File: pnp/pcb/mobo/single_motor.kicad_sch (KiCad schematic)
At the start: 9 parts, among them J26 TMC_PIN_HEADER, M2 Stepper_Motor

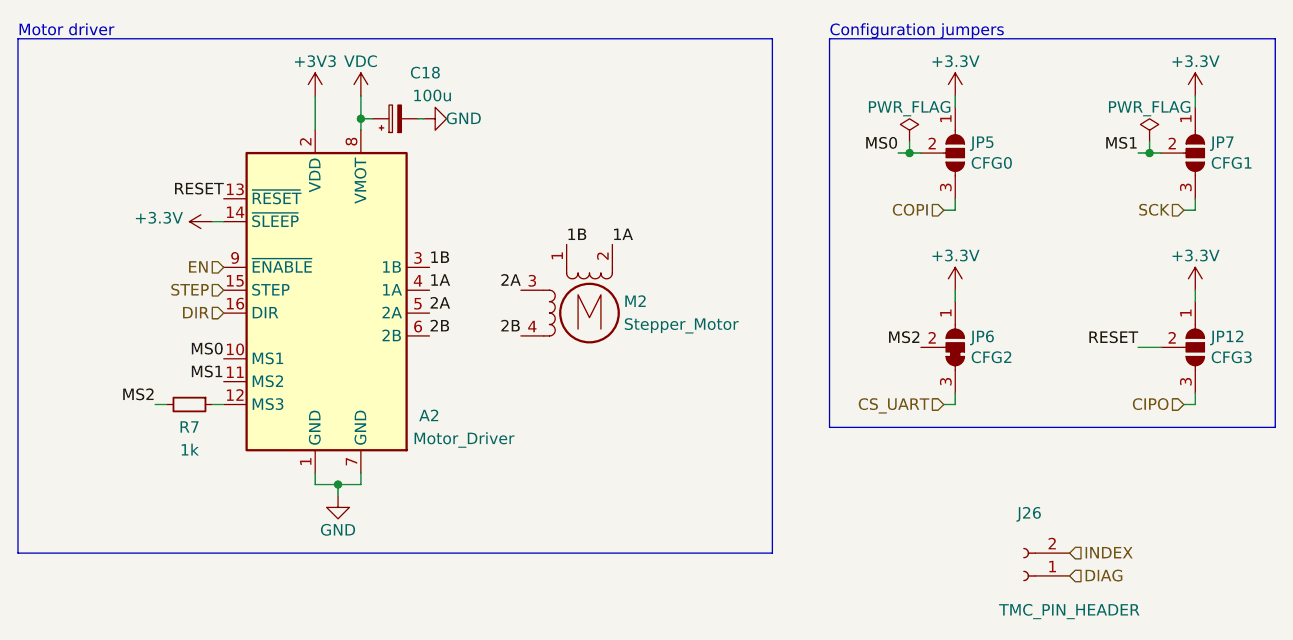
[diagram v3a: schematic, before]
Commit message: fixes erc errors about pin connectivity
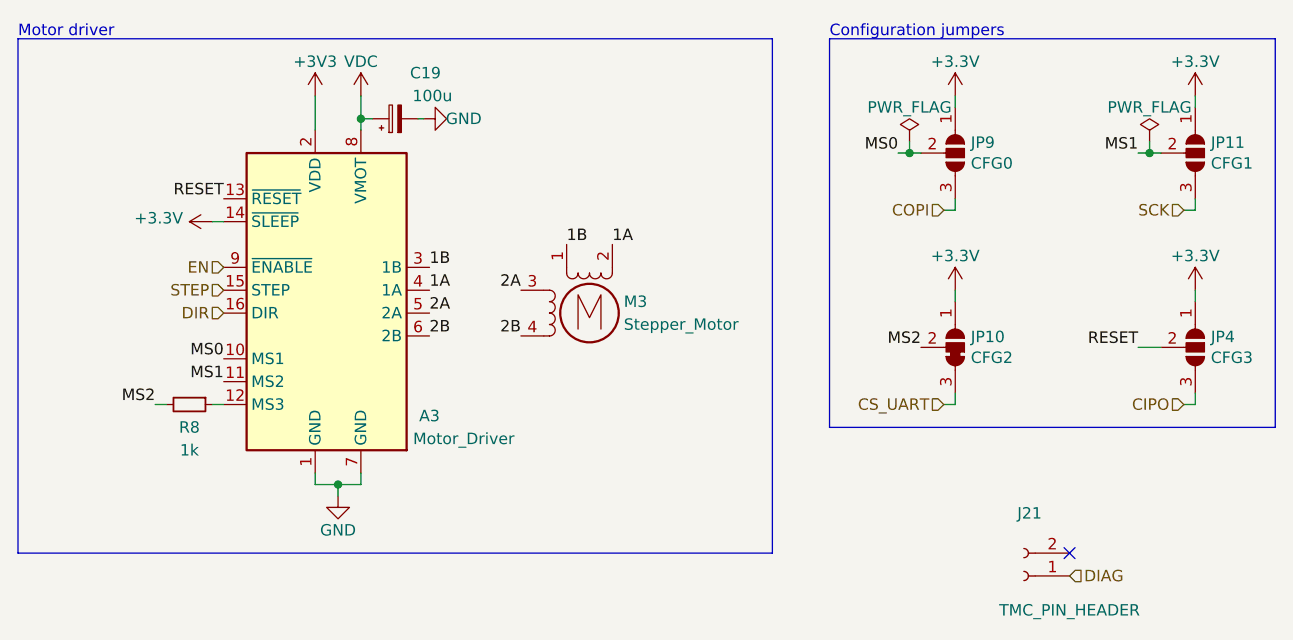
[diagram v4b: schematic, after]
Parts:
- renumbered A2 to A3, C18 to C19, J26 to J21, JP6 to JP10, JP7 to JP11, JP12 to JP4, JP5 to JP9, M2 to M3, R7 to R8
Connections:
- net INDEX: no longer names the net of J21.2 (Pin_2)
- no-connect marks 0 -> 1
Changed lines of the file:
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@@
   (junction (at 203.2 90.17) (diameter 0) (color 0 0 0 0)
   )
+  (no_connect (at 194.31 134.62))
   (wire (pts (xy 115.57 83.82) (xy 115.57 86.36))
     (stroke (width 0) (type default) (color 0 0 0 0))
@@
     (effects (font (size 1.27 1.27)) (justify right))
   )
-  (hierarchical_label "INDEX" (shape input) (at 194.31 134.62 0)
-    (effects (font (size 1.27 1.27)) (justify left))
-  )
   (hierarchical_label "COPI" (shape input) (at 180.34 96.52 180)
     (effects (font (size 1.27 1.27)) (justify right))
@@
   (symbol (lib_id "power:+3.3V") (at 208.28 105.41 0)
     (in_bom yes) (on_board yes)
-    (property "Reference" "#PWR0181" (id 0) (at 208.28 109.22 0)
+    (property "Reference" "#PWR0204" (id 0) (at 208.28 109.22 0)
       (effects (font (size 1.27 1.27)) hide)
     )
@@
   (symbol (lib_id "Device:R_Small") (at 96.52 118.11 270)
     (in_bom yes) (on_board yes)
-    (property "Reference" "R7" (id 0) (at 96.52 120.65 90))
+    (property "Reference" "R8" (id 0) (at 96.52 120.65 90))
     (property "Value" "1k" (id 1) (at 96.52 123.19 90))
     (property "Footprint" "Resistor_SMD:R_0805_2012Metric" (id 2) (at 96.52 116.332 90)
@@
   (symbol (lib_id "power:+3.3V") (at 181.61 83.82 0)
     (in_bom yes) (on_board yes)
-    (property "Reference" "#PWR0182" (id 0) (at 181.61 87.63 0)
+    (property "Reference" "#PWR0205" (id 0) (at 181.61 87.63 0)
       (effects (font (size 1.27 1.27)) hide)
     )
@@
   (symbol (lib_id "power:GND") (at 113.03 128.27 0)
     (in_bom yes) (on_board yes)
-    (property "Reference" "#PWR0202" (id 0) (at 113.03 134.62 0)
+    (property "Reference" "#PWR0211" (id 0) (at 113.03 134.62 0)
       (effects (font (size 1.27 1.27)) hide)
     )
@@
   (symbol (lib_id "power:+3.3V") (at 99.06 97.79 90)
     (in_bom yes) (on_board yes)
-    (property "Reference" "#PWR0199" (id 0) (at 102.87 97.79 0)
+    (property "Reference" "#PWR0208" (id 0) (at 102.87 97.79 0)
       (effects (font (size 1.27 1.27)) hide)
     )
@@
   (symbol (lib_id "power:PWR_FLAG") (at 203.2 88.9 0)
     (in_bom yes) (on_board yes)
-    (property "Reference" "#FLG0107" (id 0) (at 203.2 86.995 0)
+    (property "Reference" "#FLG0110" (id 0) (at 203.2 86.995 0)
       (effects (font (size 1.27 1.27)) hide)
     )
@@
   (symbol (lib_id "power:+3.3V") (at 181.61 105.41 0)
     (in_bom yes) (on_board yes)
-    (property "Reference" "#PWR0180" (id 0) (at 181.61 109.22 0)
+    (property "Reference" "#PWR0203" (id 0) (at 181.61 109.22 0)
       (effects (font (size 1.27 1.27)) hide)
     )
@@
   (symbol (lib_id "Driver_Motor:Pololu_Breakout_A4988") (at 110.49 105.41 0)
     (in_bom yes) (on_board yes)
-    (property "Reference" "A2" (id 0) (at 123.19 119.38 0))
+    (property "Reference" "A3" (id 0) (at 123.19 119.38 0))
     (property "Value" "Motor_Driver" (id 1) (at 127 121.92 0))
     (property "Footprint" "Module:Pololu_Breakout-16_15.2x20.3mm" (id 2) (at 117.475 124.46 0)
@@
   (symbol (lib_id "power:GND") (at 122.555 86.36 90)
     (in_bom yes) (on_board yes)
-    (property "Reference" "#PWR0184" (id 0) (at 128.905 86.36 0)
+    (property "Reference" "#PWR0207" (id 0) (at 128.905 86.36 0)
       (effects (font (size 1.27 1.27)) hide)
     )
@@
   (symbol (lib_id "power:+3.3V") (at 208.28 83.82 0)
     (in_bom yes) (on_board yes)
-    (property "Reference" "#PWR0183" (id 0) (at 208.28 87.63 0)
+    (property "Reference" "#PWR0206" (id 0) (at 208.28 87.63 0)
       (effects (font (size 1.27 1.27)) hide)
     )
@@
   (symbol (lib_id "power:VDC") (at 115.57 83.82 0)
     (in_bom yes) (on_board yes)
-    (property "Reference" "#PWR0201" (id 0) (at 115.57 86.36 0)
+    (property "Reference" "#PWR0210" (id 0) (at 115.57 86.36 0)
       (effects (font (size 1.27 1.27)) hide)
     )
@@
   (symbol (lib_id "Device:C_Polarized_Small") (at 119.38 86.36 90)
     (in_bom yes) (on_board yes)
-    (property "Reference" "C18" (id 0) (at 124.46 81.28 90)
+    (property "Reference" "C19" (id 0) (at 124.46 81.28 90)
       (effects (font (size 1.27 1.27)) (justify left))
     )
@@
   (symbol (lib_id "Jumper:SolderJumper_3_Open") (at 181.61 90.17 270)
     (in_bom yes) (on_board yes)
-    (property "Reference" "JP5" (id 0) (at 183.3372 89.0016 90)
+    (property "Reference" "JP9" (id 0) (at 183.3372 89.0016 90)
       (effects (font (size 1.27 1.27)) (justify left))
     )
@@
   (symbol (lib_id "power:PWR_FLAG") (at 176.53 88.9 0)
     (in_bom yes) (on_board yes)
-    (property "Reference" "#FLG0109" (id 0) (at 176.53 86.995 0)
+    (property "Reference" "#FLG0112" (id 0) (at 176.53 86.995 0)
       (effects (font (size 1.27 1.27)) hide)
     )
@@
   (symbol (lib_id "Jumper:SolderJumper_3_Open") (at 208.28 111.76 270)
     (in_bom yes) (on_board yes)
-    (property "Reference" "JP12" (id 0) (at 210.0072 110.5916 90)
+    (property "Reference" "JP4" (id 0) (at 210.0072 110.5916 90)
       (effects (font (size 1.27 1.27)) (justify left))
     )
@@
   (symbol (lib_id "power:+3V3") (at 110.49 83.82 0)
     (in_bom yes) (on_board yes)
-    (property "Reference" "#PWR0200" (id 0) (at 110.49 87.63 0)
+    (property "Reference" "#PWR0209" (id 0) (at 110.49 87.63 0)
       (effects (font (size 1.27 1.27)) hide)
     )
@@
   (symbol (lib_id "index:SolderJumper_3_Bridged23") (at 181.61 111.76 270) (mirror x)
     (in_bom yes) (on_board yes)
-    (property "Reference" "JP6" (id 0) (at 183.3372 110.5916 90)
+    (property "Reference" "JP10" (id 0) (at 183.3372 110.5916 90)
       (effects (font (size 1.27 1.27)) (justify left))
     )
@@
   (symbol (lib_id "Motor:Stepper_Motor_bipolar") (at 140.97 107.95 0)
     (in_bom yes) (on_board yes)
-    (property "Reference" "M2" (id 0) (at 144.78 106.68 0)
+    (property "Reference" "M3" (id 0) (at 144.78 106.68 0)
       (effects (font (size 1.27 1.27)) (justify left))
     )
@@
   (symbol (lib_id "Jumper:SolderJumper_3_Open") (at 208.28 90.17 270)
     (in_bom yes) (on_board yes)
-    (property "Reference" "JP7" (id 0) (at 210.0072 89.0016 90)
+    (property "Reference" "JP11" (id 0) (at 210.0072 89.0016 90)
       (effects (font (size 1.27 1.27)) (justify left))
     )
@@
   (symbol (lib_id "Connector:Conn_01x02_Female") (at 189.23 137.16 180)
     (in_bom yes) (on_board yes)
-    (property "Reference" "J26" (id 0) (at 189.865 130.1963 0))
+    (property "Reference" "J21" (id 0) (at 189.865 130.1963 0))
     (property "Value" "TMC_PIN_HEADER" (id 1) (at 194.31 140.97 0))
     (property "Footprint" "Connector_PinSocket_2.54mm:PinSocket_1x02_P2.54mm_Vertical" (id 2) (at 189.23 137.16 0)
